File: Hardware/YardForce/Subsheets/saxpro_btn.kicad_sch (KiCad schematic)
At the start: 2 parts

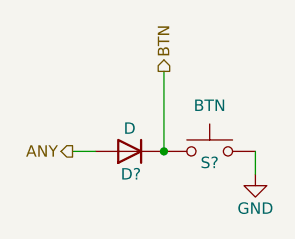
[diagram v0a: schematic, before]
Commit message: Add flash and some cleanup
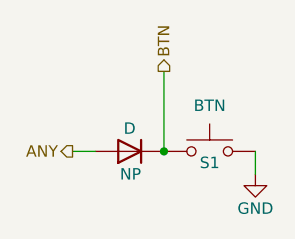
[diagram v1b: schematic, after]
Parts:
- gave numbers to parts that had none: 2
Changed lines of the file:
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@@
   (symbol (lib_id "Device:D") (at 128.27 91.44 180) (unit 1)
     (in_bom yes) (on_board yes)
-    (property "Reference" "D?" (id 0) (at 129.54 93.98 0)
+    (property "Reference" "NP" (id 0) (at 129.54 93.98 0)
       (effects (font (size 1.27 1.27)) (justify left))
     )
@@
   (symbol (lib_id "Switch:SW_Push") (at 137.16 91.44 0) (mirror y) (unit 1)
     (in_bom yes) (on_board yes)
-    (property "Reference" "S?" (id 0) (at 137.16 92.71 0))
+    (property "Reference" "S1" (id 0) (at 137.16 92.71 0))
     (property "Value" "BTN" (id 1) (at 137.16 86.36 0))
     (property "Footprint" "" (id 2) (at 137.16 86.36 0)
